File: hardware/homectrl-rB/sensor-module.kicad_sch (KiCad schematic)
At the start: 0 parts

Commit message: sensing circuitry
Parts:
- added C17, C19, C25, C26: 10uF 12V, symbol Device:C
- added C18, C20, C21, C22, C23, C24: 0.1uF 12V, symbol Device:C
- added D10, D11: SMAJ15A, Diode_SMD:D_SMA, symbol Diode:SMAJ15A
- added J3: SMS-CONN-0, symbol Connector_Generic:Conn_01x03
- added J4: SMS-CONN-1, symbol Connector_Generic:Conn_01x03
- added J5: ALS_CONN, symbol Connector_Generic:Conn_01x04
- added R12, R13, R14: 4.7k, symbol Device:R
- added R15, R16, R17, R18: 1k, symbol Device:R
- added R19, R20: 10k, symbol Device:R
- added U5: ADS1115IDGS, Package_SO:TSSOP-10_3x3mm_P0.5mm, symbol Analog_ADC:ADS1115IDGS
- added U6, U7: SI2301, TO-236_VIS, symbol SI2301:SI2301CDS-T1-GE3
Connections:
- new net: C22.2, R15.2, U5.5 (AIN1)
- new net: R17.2, U6.1 (G)
- new net: C21.1, R16.2, U5.4 (AIN0)
- new net: R18.2, U7.1 (G)
- new net +3V3: C17.1, C18.1, C19.1, C20.1, C25.1, C26.1, J5.1 (Pin_1), R12.2, R13.1, R14.1, R19.1, R20.1, U5.8 (VDD), U6.2 (S), U7.2 (S)
- new net ADC-RDY: R14.2, U5.2 (ALERT/RDY)
- new net AOUT-0: D10.1 (A1), J3.2 (Pin_2), R16.1
- new net AOUT-1: D11.1 (A1), J4.2 (Pin_2), R15.1
- new net GND: C17.2, C18.2, C19.2, C20.2, C21.2, C22.1, C23.2, C24.2, C25.2, C26.2, D10.2 (A2), D11.2 (A2), J3.3 (Pin_3), J4.3 (Pin_3), J5.4 (Pin_4), U5.1 (ADDR), U5.3 (GND)
- new net S3-SCL: J5.3 (Pin_3), R13.2, U5.10 (SCL)
- new net S3-SDA: J5.2 (Pin_2), R12.1, U5.9 (SDA)
- new net SGATE-0: R17.1, R19.2
- new net SGATE-1: R18.1, R20.2
- new net SVDD0: C23.1, J3.1 (Pin_1), U6.3 (D)
- new net SVDD1: C24.1, J4.1 (Pin_1), U7.3 (D)
- no-connect marks 0 -> 2
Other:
- note added: "0x48"
- note added: "ADC"
- note added: "S-IN"
- note added: "S-SWITCH"

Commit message: assign footprints
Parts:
- C17, C19, C21, C22, C23, C24: footprint (none) -> Capacitor_SMD:C_0603_1608Metric
- C18, C20: footprint (none) -> Capacitor_SMD:C_0402_1005Metric
- C25, C26: footprint (none) -> Capacitor_SMD:C_0805_2012Metric
- J3, J4: footprint (none) -> ul_530480310:CONN03_530480310_MOL
- J5: footprint (none) -> 530480410:MOLEX_530480410
- R12, R13, R14, R15, R16: footprint (none) -> Resistor_SMD:R_0402_1005Metric
- R17, R18, R19, R20: footprint (none) -> Resistor_SMD:R_0603_1608Metric
- U6, U7: footprint TO-236_VIS -> ul_SI2301CDS-T1-GE3:TO-236_VIS
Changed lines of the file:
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@@
 			)
 		)
-		(property "Footprint" ""
+		(property "Footprint" "Capacitor_SMD:C_0603_1608Metric"
 			(at 179.3748 134.62 0)
 			(effects
@@
 			)
 		)
-		(property "Footprint" ""
+		(property "Footprint" "Resistor_SMD:R_0603_1608Metric"
 			(at 56.388 142.24 90)
 			(effects
@@
 			)
 		)
-		(property "Footprint" ""
+		(property "Footprint" "Resistor_SMD:R_0603_1608Metric"
 			(at 58.42 116.078 90)
 			(effects
@@
 			)
 		)
-		(property "Footprint" ""
+		(property "Footprint" "Capacitor_SMD:C_0603_1608Metric"
 			(at 49.2252 68.58 0)
 			(effects
@@
 			)
 		)
-		(property "Footprint" ""
+		(property "Footprint" "Resistor_SMD:R_0402_1005Metric"
 			(at 172.72 136.398 90)
 			(effects
@@
 			)
 		)
-		(property "Footprint" ""
+		(property "Footprint" "Capacitor_SMD:C_0603_1608Metric"
 			(at 121.6152 81.28 0)
 			(effects
@@
 			)
 		)
-		(property "Footprint" ""
+		(property "Footprint" "ul_530480310:CONN03_530480310_MOL"
 			(at 55.88 55.88 0)
 			(effects
@@
 			)
 		)
-		(property "Footprint" ""
+		(property "Footprint" "Resistor_SMD:R_0402_1005Metric"
 			(at 172.72 133.858 90)
 			(effects
@@
 			)
 		)
-		(property "Footprint" ""
+		(property "Footprint" "Capacitor_SMD:C_0805_2012Metric"
 			(at 116.84 141.2748 0)
 			(effects
@@
 			)
 		)
-		(property "Footprint" ""
+		(property "Footprint" "Capacitor_SMD:C_0603_1608Metric"
 			(at 82.2452 68.58 0)
 			(effects
@@
 			)
 		)
-		(property "Footprint" ""
+		(property "Footprint" "Capacitor_SMD:C_0603_1608Metric"
 			(at 179.3748 124.46 0)
 			(effects
@@
 			)
 		)
-		(property "Footprint" ""
+		(property "Footprint" "Resistor_SMD:R_0402_1005Metric"
 			(at 219.202 130.81 90)
 			(effects
@@
 			)
 		)
-		(property "Footprint" ""
+		(property "Footprint" "Capacitor_SMD:C_0603_1608Metric"
 			(at 193.3448 111.76 0)
 			(effects
@@
 			)
 		)
-		(property "Footprint" ""
+		(property "Footprint" "Resistor_SMD:R_0402_1005Metric"
 			(at 206.502 125.73 90)
 			(effects
@@
 			)
 		)
-		(property "Footprint" ""
+		(property "Footprint" "Capacitor_SMD:C_0402_1005Metric"
 			(at 188.2648 111.76 0)
 			(effects
@@
 			)
 		)
-		(property "Footprint" ""
+		(property "Footprint" "Capacitor_SMD:C_0402_1005Metric"
 			(at 134.3152 81.28 0)
 			(effects
@@
 			)
 		)
-		(property "Footprint" ""
+		(property "Footprint" "Resistor_SMD:R_0402_1005Metric"
 			(at 219.202 140.97 90)
 			(effects
@@
 			)
 		)
-		(property "Footprint" ""
+		(property "Footprint" "530480410:MOLEX_530480410"
 			(at 123.19 55.88 0)
 			(effects
@@
 			)
 		)
-		(property "Footprint" ""
+		(property "Footprint" "Resistor_SMD:R_0603_1608Metric"
 			(at 58.42 140.208 90)
 			(effects
@@
 			)
 		)
-		(property "Footprint" "TO-236_VIS"
+		(property "Footprint" "ul_SI2301CDS-T1-GE3:TO-236_VIS"
 			(at 62.23 138.43 0)
 			(effects
@@
 			)
 		)
-		(property "Footprint" ""
+		(property "Footprint" "Capacitor_SMD:C_0805_2012Metric"
 			(at 115.57 114.6048 0)
 			(effects
@@
 			)
 		)
-		(property "Footprint" "TO-236_VIS"
+		(property "Footprint" "ul_SI2301CDS-T1-GE3:TO-236_VIS"
 			(at 62.23 114.3 0)
 			(effects
@@
 			)
 		)
-		(property "Footprint" ""
+		(property "Footprint" "ul_530480310:CONN03_530480310_MOL"
 			(at 88.9 55.88 0)
 			(effects
@@
 			)
 		)
-		(property "Footprint" ""
+		(property "Footprint" "Resistor_SMD:R_0603_1608Metric"
 			(at 56.388 118.11 90)
 			(effects

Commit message: W
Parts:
- C17, C18, C19, C20, C21, C22, C23, C24, C25, C26, D10, D11, U5, U6, U7: Purchase (none) -> Yes
- J3, J4, J5: Purchase (none) -> No
- R12, R13, R14, R15, R16, R17, R18, R19, R20: Purchase (none) -> N/A

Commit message: add new caps, add ferrite bead, add MPNs
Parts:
- D10, D11: MPN (none) -> SMAJ15A
- J3, J4, J5: MPN (none) -> N/A
- R12, R13, R14, R15, R16, R17, R18, R19, R20: Purchase N/A -> Yes
- U5: MPN (none) -> ADS1115IDGSR
- U6, U7: MPN (none) -> SI2301CDS-T1-GE3
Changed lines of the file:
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@@
 			)
 		)
-		(property "Purchase" "N/A"
+		(property "Purchase" "Yes"
 			(at 54.61 142.24 0)
 			(effects
@@
 			)
 		)
-		(property "Purchase" "N/A"
+		(property "Purchase" "Yes"
 			(at 58.42 114.3 0)
 			(effects
@@
 			)
 		)
-		(property "Purchase" "N/A"
+		(property "Purchase" "Yes"
 			(at 172.72 134.62 0)
 			(effects
@@
 			)
 		)
-		(property "MPN" ""
+		(property "MPN" "N/A"
 			(at 55.88 55.88 0)
 			(effects
@@
 			)
 		)
-		(property "Purchase" "N/A"
+		(property "Purchase" "Yes"
 			(at 172.72 132.08 0)
 			(effects
@@
 			)
 		)
-		(property "MPN" ""
+		(property "MPN" "ADS1115IDGSR"
 			(at 194.31 134.62 0)
 			(effects
@@
 			)
 		)
-		(property "MPN" ""
+		(property "MPN" "SMAJ15A"
 			(at 92.71 68.58 0)
 			(effects
@@
 			)
 		)
-		(property "Purchase" "N/A"
+		(property "Purchase" "Yes"
 			(at 220.98 130.81 0)
 			(effects
@@
 			)
 		)
-		(property "Purchase" "N/A"
+		(property "Purchase" "Yes"
 			(at 208.28 125.73 0)
 			(effects
@@
 			)
 		)
-		(property "MPN" ""
+		(property "MPN" "SMAJ15A"
 			(at 59.69 69.85 0)
 			(effects
@@
 			)
 		)
-		(property "Purchase" "N/A"
+		(property "Purchase" "Yes"
 			(at 220.98 140.97 0)
 			(effects
@@
 			)
 		)
-		(property "MPN" ""
+		(property "MPN" "N/A"
 			(at 123.19 55.88 0)
 			(effects
@@
 			)
 		)
-		(property "Purchase" "N/A"
+		(property "Purchase" "Yes"
 			(at 58.42 138.43 0)
 			(effects
@@
 			)
 		)
-		(property "MPN" ""
+		(property "MPN" "SI2301CDS-T1-GE3"
 			(at 62.23 138.43 0)
 			(effects
@@
 			)
 		)
-		(property "MPN" ""
+		(property "MPN" "SI2301CDS-T1-GE3"
 			(at 62.23 114.3 0)
 			(effects
@@
 			)
 		)
-		(property "MPN" ""
+		(property "MPN" "N/A"
 			(at 88.9 55.88 0)
 			(effects
@@
 			)
 		)
-		(property "Purchase" "N/A"
+		(property "Purchase" "Yes"
 			(at 54.61 118.11 0)
 			(effects

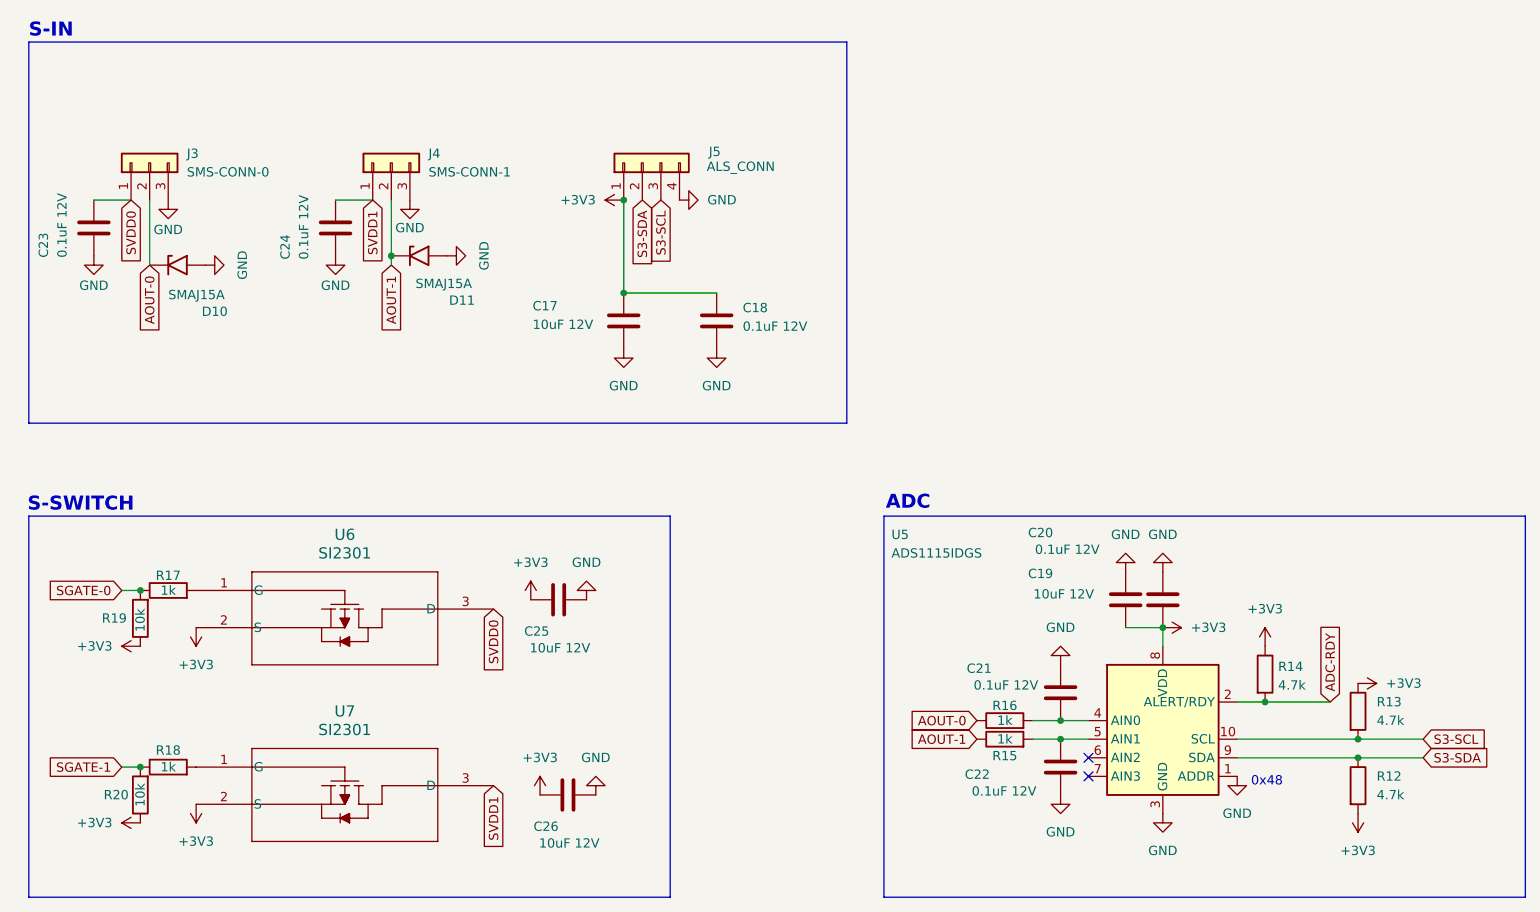
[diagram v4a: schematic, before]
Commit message: add MPNs and review circuits
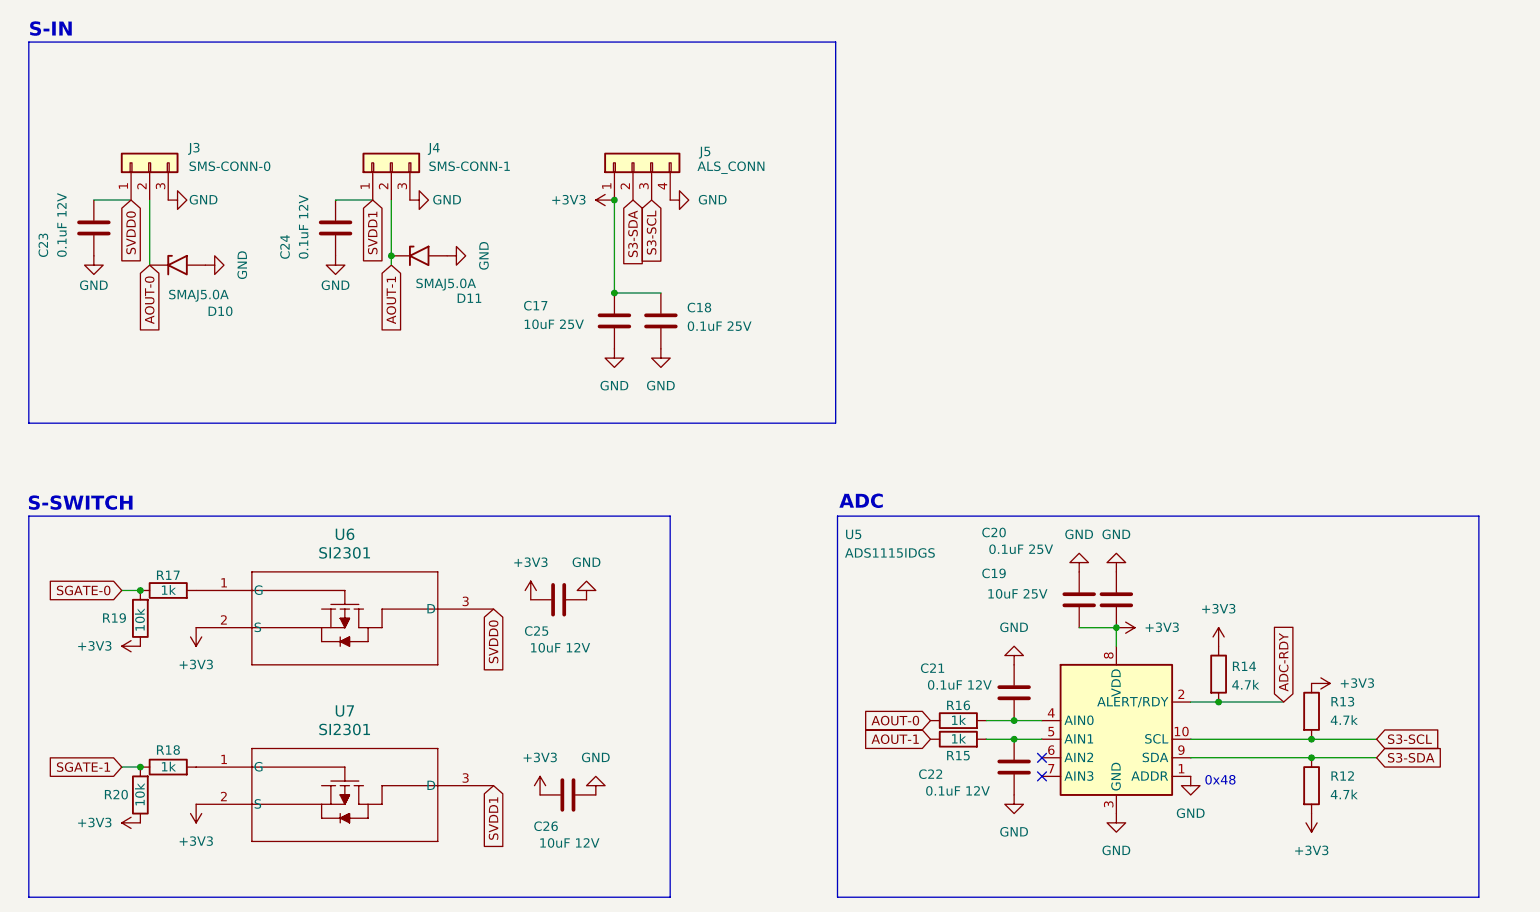
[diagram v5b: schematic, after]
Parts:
- C17, C19: value 10uF 12V -> 10uF 25V; MPN (none) -> GRM188R61E106MA73D
- C18, C20: value 0.1uF 12V -> 0.1uF 25V; MPN (none) -> GRM155R71E104KE14D
- C21, C22, C23, C24: MPN (none) -> CL10B104KA8NNNC
- C25, C26: MPN (none) -> GRT188R61C106KE13D
- D10, D11: value SMAJ15A -> SMAJ5.0A
- R12, R13, R14: MPN (none) -> RC0402FR-074K7L
- R15, R16: MPN (none) -> ERJ-2RKF1001X
- R17, R18: MPN (none) -> ERJ-3EKF1001V
- R19, R20: MPN (none) -> ERJ-3EKF1002V
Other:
- moved on the sheet: C17, C18, C19, C20, C21, C22, J5, R12, R13, R14, R15, R16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

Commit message: swap connector in progress
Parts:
- removed D10, D11: SMAJ5.0A, Diode_SMD:D_SMA, symbol Diode:SMAJ15A
- added C14: 0.1uF, Capacitor_SMD:C_0603_1608Metric, symbol Device:C
- added U9: TPD2E001DRLR, TPD2E001DRLR:SOT50P160X60-5N, symbol TPD2E001DRLR:TPD2E001DRLR
- C17, C19: value 10uF 25V -> 10uF
- C18, C20: value 0.1uF 25V -> 0.1uF
- C21, C22, C23, C24: value 0.1uF 12V -> 0.1uF
- C25, C26: value 10uF 12V -> 10uF; MPN GRT188R61C106KE13D -> CL21B106KOQNNN
- J3, J4: footprint ul_530480310:CONN03_530480310_MOL -> LIB_S03B-PASK-2_LF__SN_:S03BPASK2LFSN
- J5: footprint 530480410:MOLEX_530480410 -> S04B_PASK_2:CONN4_S04B-PASK_JST
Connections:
- net +3V3: now also C14.2, U9.1 (VCC)
- net AOUT-0: now also U9.3 (IO1)
- net AOUT-1: now also U9.5 (IO2)
- net GND: now also C14.1, U9.4 (GND)
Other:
- note added: "S-PROT"
- moved on the sheet: C17, C18, C24, J4, J5

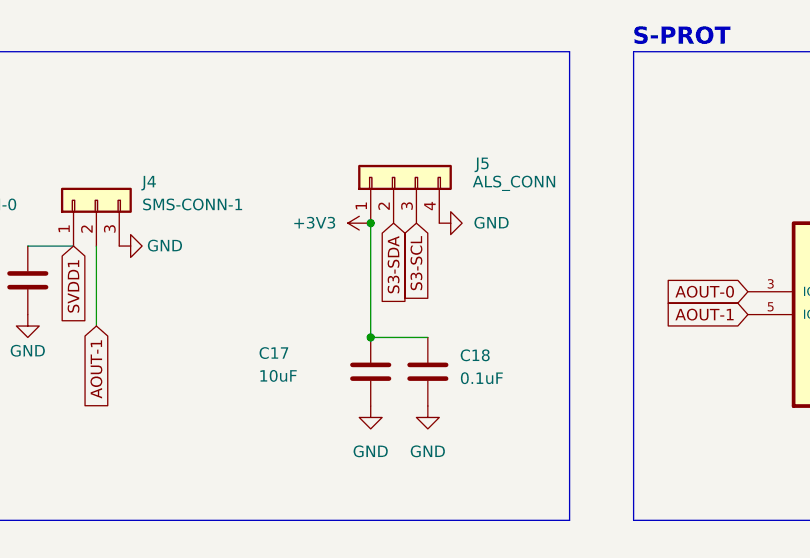
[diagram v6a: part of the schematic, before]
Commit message: connector fixes
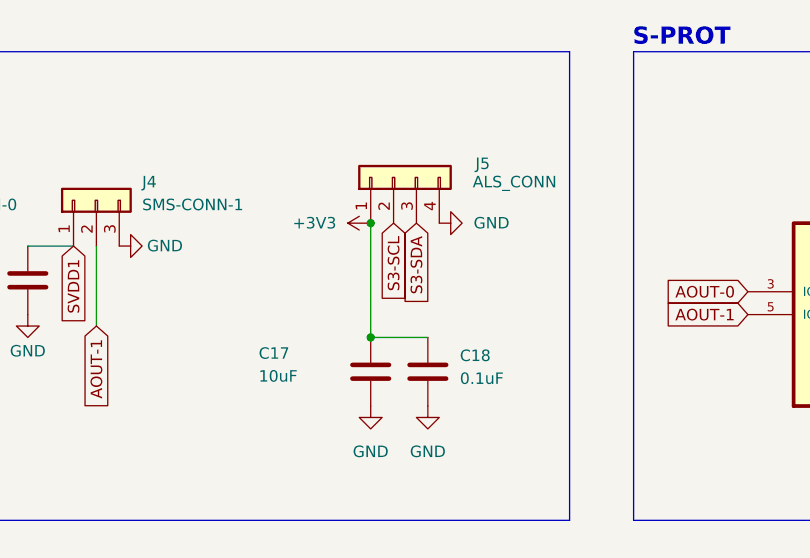
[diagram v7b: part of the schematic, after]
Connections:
- net S3-SCL: now also J5.2 (Pin_2); no longer J5.3 (Pin_3)
- net S3-SDA: now also J5.3 (Pin_3); no longer J5.2 (Pin_2)

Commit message: BOM fix
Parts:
- C17, C19, C25, C26: value 10uF -> 10uF
- C18, C20, C21, C22, C23, C24: value 0.1uF -> 0.1uF
- J3, J4: MPN N/A -> S03B-PASK-2; Purchase No -> Yes
- J5: MPN N/A -> S04B-PASK-2; Purchase No -> Yes
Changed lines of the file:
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@@
 			)
 		)
-		(property "Value" "0.1uF "
+		(property "Value" "0.1uF"
 			(at 170.688 141.732 0)
 			(effects
@@
 			)
 		)
-		(property "Value" "0.1uF "
+		(property "Value" "0.1uF"
 			(at 43.942 68.834 90)
 			(effects
@@
 			)
 		)
-		(property "Value" "10uF "
+		(property "Value" "10uF"
 			(at 99.314 75.438 0)
 			(effects
@@
 			)
 		)
-		(property "MPN" "N/A"
+		(property "MPN" "  S03B-PASK-2"
 			(at 55.88 55.88 0)
 			(effects
@@
 			)
 		)
-		(property "Purchase" "No"
+		(property "Purchase" "Yes"
 			(at 55.88 55.88 0)
 			(effects
@@
 			)
 		)
-		(property "Value" "10uF "
+		(property "Value" "10uF"
 			(at 117.348 148.844 90)
 			(effects
@@
 			)
 		)
-		(property "Value" "0.1uF "
+		(property "Value" "0.1uF"
 			(at 69.342 69.088 90)
 			(effects
@@
 			)
 		)
-		(property "Value" "0.1uF "
+		(property "Value" "0.1uF"
 			(at 170.942 127.254 0)
 			(effects
@@
 			)
 		)
-		(property "Value" "10uF "
+		(property "Value" "10uF"
 			(at 178.562 114.808 0)
 			(effects
@@
 			)
 		)
-		(property "Value" "0.1uF "
+		(property "Value" "0.1uF"
 			(at 179.324 108.712 0)
 			(effects
@@
 			)
 		)
-		(property "Value" "0.1uF "
+		(property "Value" "0.1uF"
 			(at 121.666 75.692 0)
 			(effects
@@
 			)
 		)
-		(property "MPN" "N/A"
+		(property "MPN" "  S04B-PASK-2"
 			(at 114.3 53.34 0)
 			(effects
@@
 			)
 		)
-		(property "Purchase" "No"
+		(property "Purchase" "Yes"
 			(at 114.3 53.34 0)
 			(effects
@@
 			)
 		)
-		(property "Value" "10uF "
+		(property "Value" "10uF"
 			(at 116.078 122.174 90)
 			(effects
@@
 			)
 		)
-		(property "MPN" "N/A"
+		(property "MPN" "  S03B-PASK-2"
 			(at 81.28 55.88 0)
 			(effects
@@
 			)
 		)
-		(property "Purchase" "No"
+		(property "Purchase" "Yes"
 			(at 81.28 55.88 0)
 			(effects
